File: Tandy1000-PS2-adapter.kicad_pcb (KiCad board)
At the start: 2 copper layers, 50 x 19 mm, 11 parts, among them J1 Mini-DIN-6, J2 Conn_01x05, U1 ATtiny85

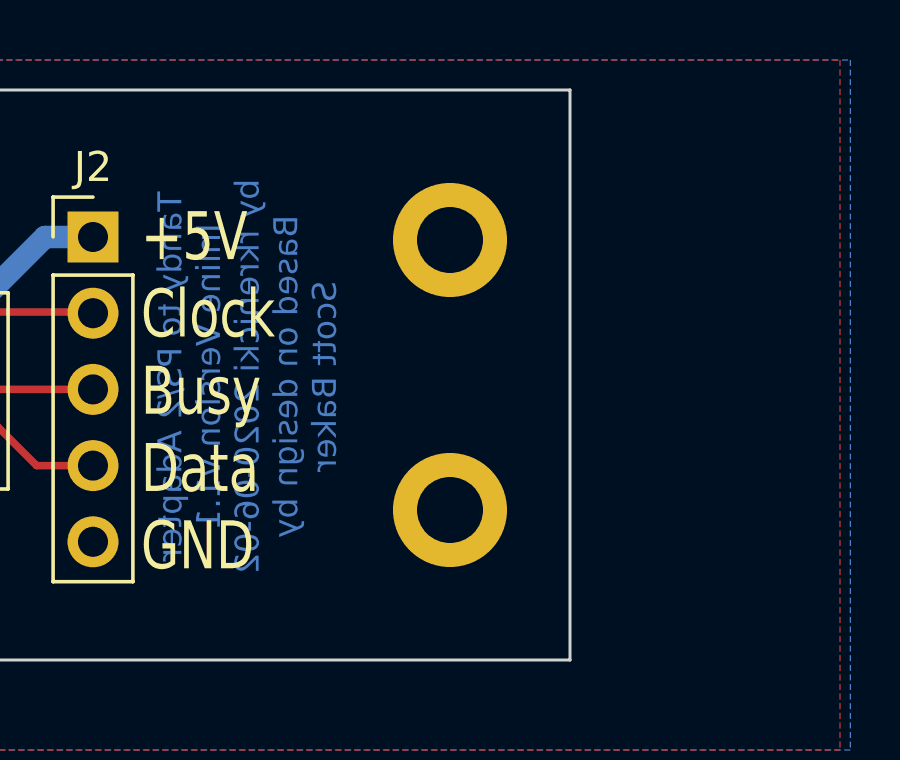
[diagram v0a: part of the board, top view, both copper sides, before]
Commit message: 1.2 Update
Enlarged mounting holes to 2.7mm for more zip-tie compatibility.
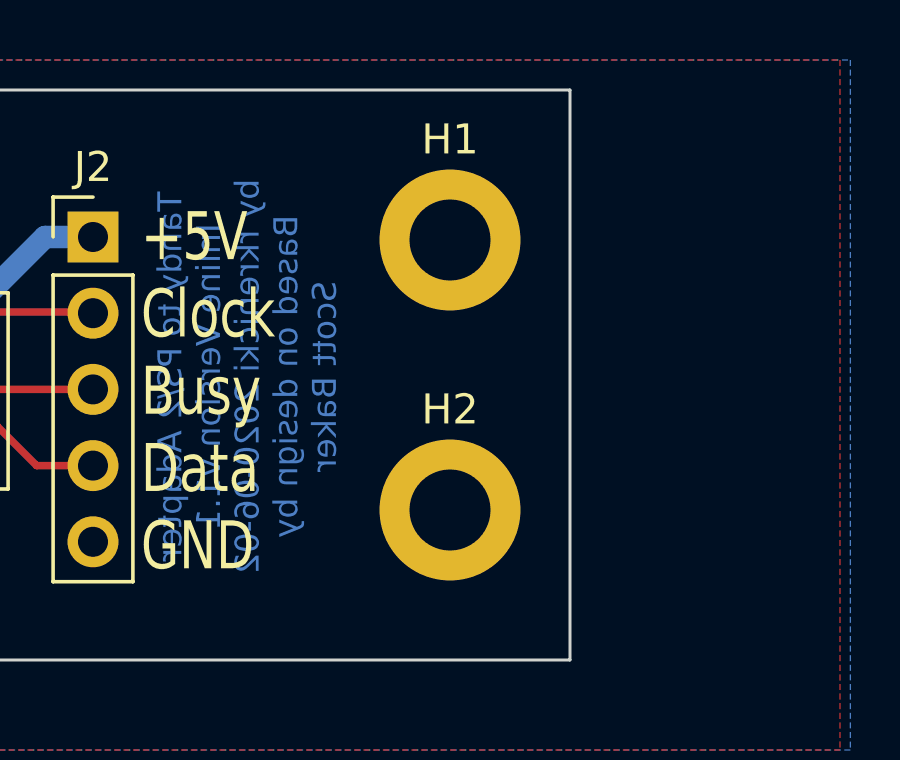
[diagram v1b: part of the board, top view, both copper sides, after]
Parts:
- H1, H2: footprint MountingHole:MountingHole_2.2mm_M2_DIN965_Pad -> MountingHole:MountingHole_2.7mm_M2.5_DIN965_Pad
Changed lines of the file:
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@@
   )
   (setup
-    (last_trace_width 0.75)
+    (last_trace_width 0.25)
     (user_trace_width 0.75)
     (trace_clearance 0.2)
@@
     (visible_elements 7FFFFFFF)
     (pcbplotparams
-      (layerselection 0x010fc_ffffffff)
+      (layerselection 0x010f0_ffffffff)
       (usegerberextensions false)
       (usegerberattributes false)
@@
     (add_net Tandy-DATA)
   )
+  (module MountingHole:MountingHole_2.7mm_M2.5_DIN965_Pad (layer F.Cu)
+    (at 152 70)
+    (descr "Mounting Hole 2.7mm, M2.5, DIN965")
+    (tags "mounting hole 2.7mm m2.5 din965")
+    (attr virtual)
+    (fp_text reference H2 (at 0 -3.35) (layer F.SilkS)
+      (effects (font (size 1 1) (thickness 0.15)))
+    )
+    (fp_text value MountingHole_Pad (at 0 3.35) (layer F.Fab)
+      (effects (font (size 1 1) (thickness 0.15)))
+    )
+    (fp_circle (center 0 0) (end 2.6 0) (layer F.CrtYd) (width 0.05))
+    (fp_circle (center 0 0) (end 2.35 0) (layer Cmts.User) (width 0.15))
+    (fp_text user %R (at 0.3 0) (layer F.Fab)
+      (effects (font (size 1 1) (thickness 0.15)))
+    )
+    (pad 1 thru_hole circle (at 0 0) (size 4.7 4.7) (drill 2.7) (layers *.Cu *.Mask)
+      (net 1 GND))
+  )
+  (module MountingHole:MountingHole_2.7mm_M2.5_DIN965_Pad (layer F.Cu)
+    (at 152 61)
+    (descr "Mounting Hole 2.7mm, M2.5, DIN965")
+    (tags "mounting hole 2.7mm m2.5 din965")
+    (attr virtual)
+    (fp_text reference H1 (at 0 -3.35) (layer F.SilkS)
+      (effects (font (size 1 1) (thickness 0.15)))
+    )
+    (fp_text value MountingHole_Pad (at 0 3.35) (layer F.Fab)
+      (effects (font (size 1 1) (thickness 0.15)))
+    )
+    (fp_circle (center 0 0) (end 2.6 0) (layer F.CrtYd) (width 0.05))
+    (fp_circle (center 0 0) (end 2.35 0) (layer Cmts.User) (width 0.15))
+    (fp_text user %R (at 0.3 0) (layer F.Fab)
+      (effects (font (size 1 1) (thickness 0.15)))
+    )
+    (pad 1 thru_hole circle (at 0 0) (size 4.7 4.7) (drill 2.7) (layers *.Cu *.Mask)
+      (net 1 GND))
+  )
   (module Resistor_THT:R_Axial_DIN0207_L6.3mm_D2.5mm_P10.16mm_Horizontal (layer F.Cu)
     (at 135.9 71.11 90)
@@
     )
   )
-  (module MountingHole:MountingHole_2.2mm_M2_DIN965_Pad (layer F.Cu)
-    (at 152 70)
-    (descr "Mounting Hole 2.2mm, M2, DIN965")
-    (tags "mounting hole 2.2mm m2 din965")
-    (attr virtual)
-    (fp_text reference H2 (at 0 -2.9) (layer F.SilkS) hide
-      (effects (font (size 1 1) (thickness 0.15)))
-    )
-    (fp_text value MountingHole_Pad (at 0 2.9) (layer F.Fab)
-      (effects (font (size 1 1) (thickness 0.15)))
-    )
-    (fp_circle (center 0 0) (end 2.15 0) (layer F.CrtYd) (width 0.05))
-    (fp_circle (center 0 0) (end 1.9 0) (layer Cmts.User) (width 0.15))
-    (fp_text user %R (at 0.3 0) (layer F.Fab)
-      (effects (font (size 1 1) (thickness 0.15)))
-    )
-    (pad 1 thru_hole circle (at 0 0) (size 3.8 3.8) (drill 2.2) (layers *.Cu *.Mask)
-      (net 1 GND))
-  )
-  (module MountingHole:MountingHole_2.2mm_M2_DIN965_Pad (layer F.Cu)
-    (at 152 61)
-    (descr "Mounting Hole 2.2mm, M2, DIN965")
-    (tags "mounting hole 2.2mm m2 din965")
-    (attr virtual)
-    (fp_text reference H1 (at 0 -2.9) (layer F.SilkS) hide
-      (effects (font (size 1 1) (thickness 0.15)))
-    )
-    (fp_text value MountingHole_Pad (at 0 2.9) (layer F.Fab)
-      (effects (font (size 1 1) (thickness 0.15)))
-    )
-    (fp_circle (center 0 0) (end 2.15 0) (layer F.CrtYd) (width 0.05))
-    (fp_circle (center 0 0) (end 1.9 0) (layer Cmts.User) (width 0.15))
-    (fp_text user %R (at 0.3 0) (layer F.Fab)
-      (effects (font (size 1 1) (thickness 0.15)))
-    )
-    (pad 1 thru_hole circle (at 0 0) (size 3.8 3.8) (drill 2.2) (layers *.Cu *.Mask)
-      (net 1 GND))
-  )
   (module Connector_PinHeader_2.54mm:PinHeader_1x05_P2.54mm_Vertical (layer F.Cu)
